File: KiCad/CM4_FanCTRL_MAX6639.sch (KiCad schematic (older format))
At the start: 14 parts, among them M1 Fan_CPU_4pin, M2 Fan_CPU_4pin, U1 MAX6639ATE+

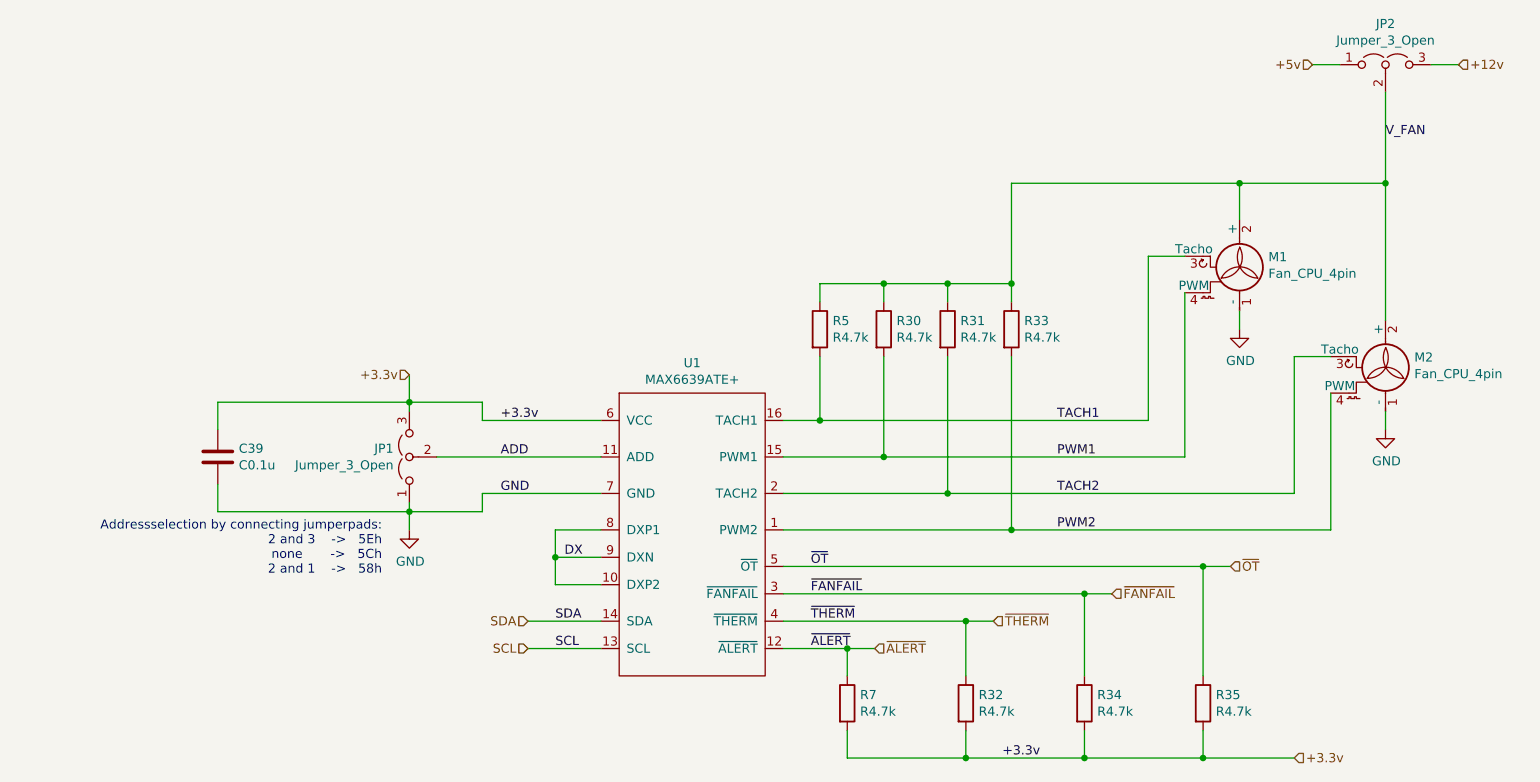
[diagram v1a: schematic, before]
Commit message: PCIe Wiring, resistor value adjustments, and a bunch of small ERC fixes.
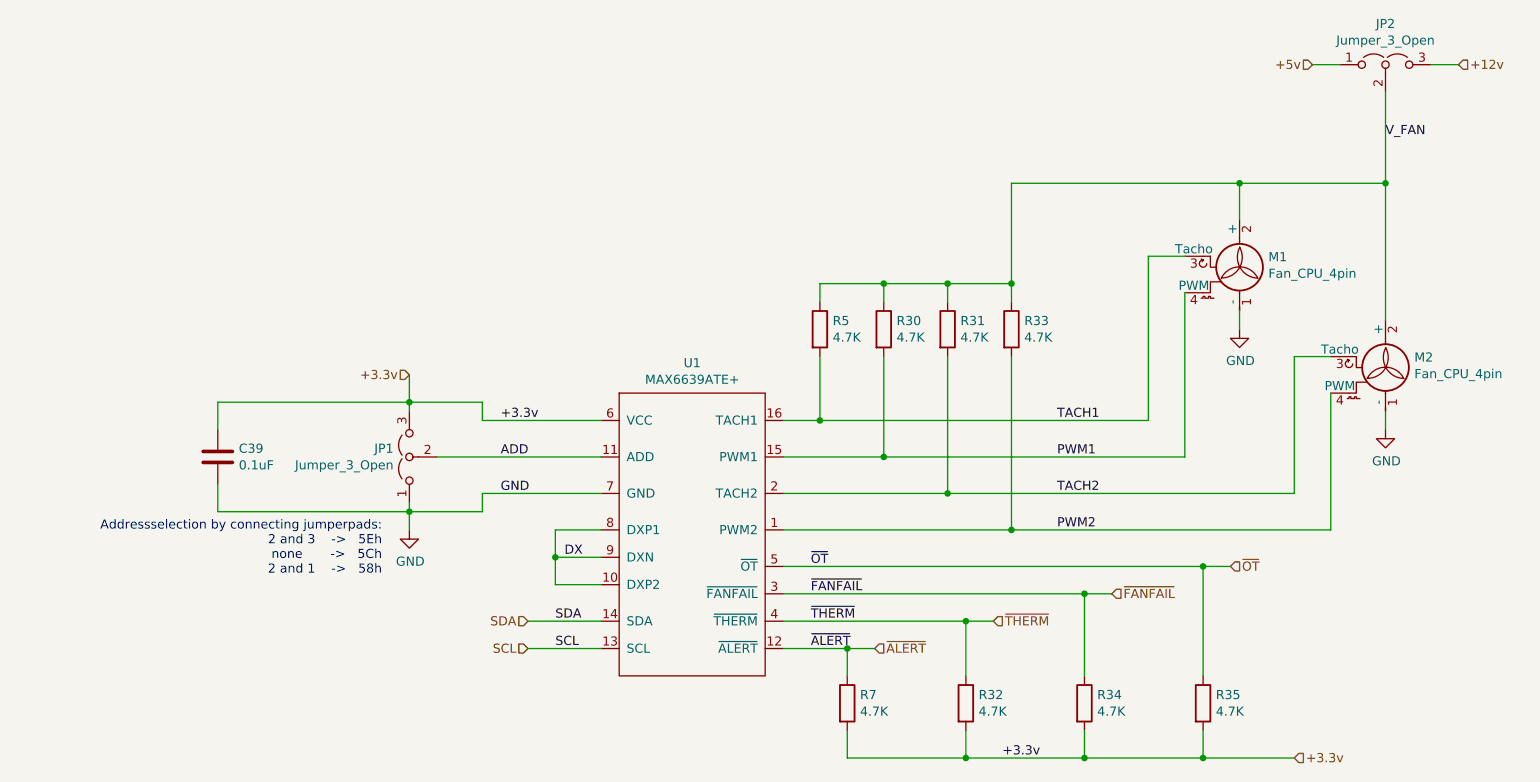
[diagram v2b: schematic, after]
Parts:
- C39: value C0.1u -> 0.1uF
- R30, R31, R32, R33, R34, R35, R5, R7: value R4.7k -> 4.7K
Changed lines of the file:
@@
 P 5750 5350
 F 0 "R7" H 5820 5396 50  0000 L CNN
-F 1 "R4.7k" H 5820 5305 50  0000 L CNN
+F 1 "4.7K" H 5820 5305 50  0000 L CNN
 F 2 "CM4_MATX:R_0805_2012Metric_Pad1.20x1.40mm_HandSolder" V 5680 5350 50  0001 C CNN
 F 3 "~" H 5750 5350 50  0001 C CNN
@@
 P 6400 5350
 F 0 "R32" H 6470 5396 50  0000 L CNN
-F 1 "R4.7k" H 6470 5305 50  0000 L CNN
+F 1 "4.7K" H 6470 5305 50  0000 L CNN
 F 2 "CM4_MATX:R_0805_2012Metric_Pad1.20x1.40mm_HandSolder" V 6330 5350 50  0001 C CNN
 F 3 "~" H 6400 5350 50  0001 C CNN
@@
 P 7050 5350
 F 0 "R34" H 7120 5396 50  0000 L CNN
-F 1 "R4.7k" H 7120 5305 50  0000 L CNN
+F 1 "4.7K" H 7120 5305 50  0000 L CNN
 F 2 "CM4_MATX:R_0805_2012Metric_Pad1.20x1.40mm_HandSolder" V 6980 5350 50  0001 C CNN
 F 3 "~" H 7050 5350 50  0001 C CNN
@@
 P 7700 5350
 F 0 "R35" H 7770 5396 50  0000 L CNN
-F 1 "R4.7k" H 7770 5305 50  0000 L CNN
+F 1 "4.7K" H 7770 5305 50  0000 L CNN
 F 2 "CM4_MATX:R_0805_2012Metric_Pad1.20x1.40mm_HandSolder" V 7630 5350 50  0001 C CNN
 F 3 "~" H 7700 5350 50  0001 C CNN
@@
 P 6300 3300
 F 0 "R31" H 6370 3346 50  0000 L CNN
-F 1 "R4.7k" H 6370 3255 50  0000 L CNN
+F 1 "4.7K" H 6370 3255 50  0000 L CNN
 F 2 "CM4_MATX:R_0805_2012Metric_Pad1.20x1.40mm_HandSolder" V 6230 3300 50  0001 C CNN
 F 3 "~" H 6300 3300 50  0001 C CNN
@@
 P 6650 3300
 F 0 "R33" H 6720 3346 50  0000 L CNN
-F 1 "R4.7k" H 6720 3255 50  0000 L CNN
+F 1 "4.7K" H 6720 3255 50  0000 L CNN
 F 2 "CM4_MATX:R_0805_2012Metric_Pad1.20x1.40mm_HandSolder" V 6580 3300 50  0001 C CNN
 F 3 "~" H 6650 3300 50  0001 C CNN
@@
 P 5600 3300
 F 0 "R5" H 5670 3346 50  0000 L CNN
-F 1 "R4.7k" H 5670 3255 50  0000 L CNN
+F 1 "4.7K" H 5670 3255 50  0000 L CNN
 F 2 "CM4_MATX:R_0805_2012Metric_Pad1.20x1.40mm_HandSolder" V 5530 3300 50  0001 C CNN
 F 3 "~" H 5600 3300 50  0001 C CNN
@@
 P 5950 3300
 F 0 "R30" H 6020 3346 50  0000 L CNN
-F 1 "R4.7k" H 6020 3255 50  0000 L CNN
+F 1 "4.7K" H 6020 3255 50  0000 L CNN
 F 2 "CM4_MATX:R_0805_2012Metric_Pad1.20x1.40mm_HandSolder" V 5880 3300 50  0001 C CNN
 F 3 "~" H 5950 3300 50  0001 C CNN
@@
 P 2300 4000
 F 0 "C39" H 2415 4046 50  0000 L CNN
-F 1 "C0.1u" H 2415 3955 50  0000 L CNN
+F 1 "0.1uF" H 2415 3955 50  0000 L CNN
 F 2 "CM4_MATX:C_0805_2012Metric_Pad1.18x1.45mm_HandSolder" H 2338 3850 50  0001 C CNN
 F 3 "~" H 2300 4000 50  0001 C CNN

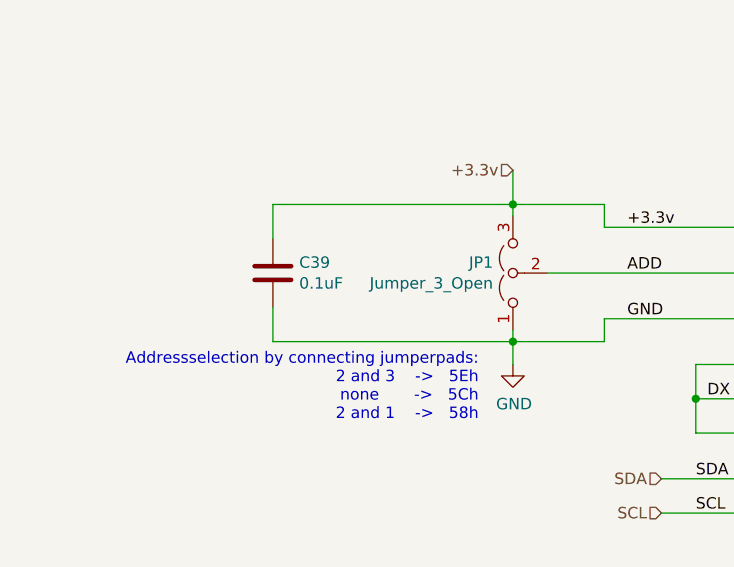
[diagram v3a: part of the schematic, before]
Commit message: Started picking passive components, overhauled library
Cleaned up a bunch of schematic library references.
Added datasheets, descriptions for a lot of existing parts.
Picked most capacitor parts, still a couple left.
Cleaned up a fair few footprint references.
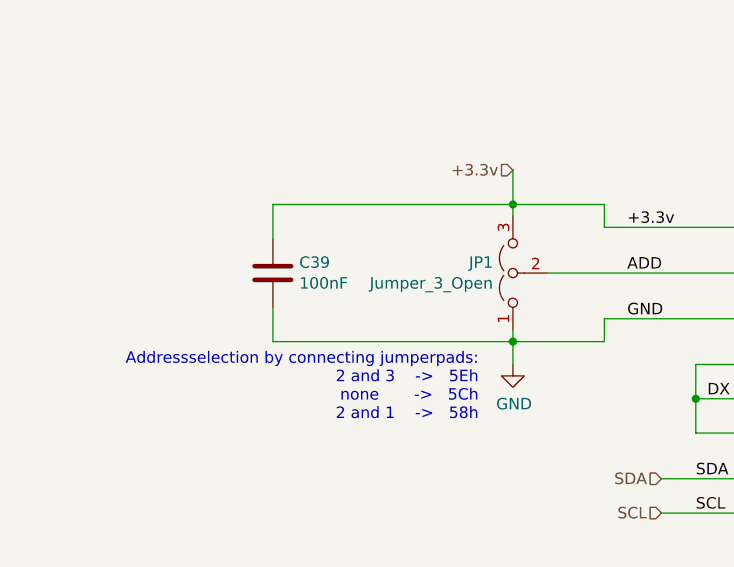
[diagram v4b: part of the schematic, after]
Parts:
- C39: value 0.1uF -> 100nF; footprint CM4_MATX:C_0805_2012Metric_Pad1.18x1.45mm_HandSolder -> CM4_MATX:C_0402_1005Metric_Pad0.74x0.62mm_HandSolder; Description (none) -> 10V 0.1uF X5R 0402 20% Tol; Mfr. (none) -> AVX; Mfr. No (none) -> 0402ZD104MAT4A; Mouser Part Number (none) -> 581-0402ZD104MAT4A; Mouser Price/Stock (none) -> https://www.mouser.co.uk/ProductDetail/AVX/0402ZD104MAT4A/?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
- JP1, JP2: Description (none) -> Standard 2.54mm (100mil)-separated pins
- U1: Description (none) -> 2-Channel Temperature Monitor with Dual, Automatic, PWM Fan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; Mfr. No (none) -> MAX6639ATE+; Mfr. No. MAX6639ATE+ -> (none); Mouser No. 700-MAX6639ATE -> (none); Mouser Part Number (none) -> 700-MAX6639ATE; Mouser Price/Stock (none) -> https://www.mouser.co.uk/ProductDetail/Maxim-Integrated/MAX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
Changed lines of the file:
@@
 F 2 "CM4_MATX:TQFN-16-1EP_5x5mm_P0.8mm_EP3.1x3.1mm" H 4950 5800 50  0001 C CNN
 F 3 "https://datasheets.maximintegrated.com/en/ds/MAX6639-MAX6639F.pdf" H 4900 5500 50  0001 C CNN
-F 4 "700-MAX6639ATE" H 4900 5700 50  0001 C CNN "Mouser No."
-F 5 "Maxim Integrated" H 4900 5700 50  0001 C CNN "Mfr."
-F 6 "MAX6639ATE+" H 4900 5350 50  0001 C CNN "Mfr. No."
+F 4 "Maxim Integrated" H 4900 5700 50  0001 C CNN "Mfr."
+F 5 "MAX6639ATE+" H 4900 4450 50  0001 C CNN "Mfr. No"
+F 6 "700-MAX6639ATE" H 4900 4450 50  0001 C CNN "Mouser Part Number"
+F 7 "https://www.mouser.co.uk/ProductDetail/Maxim-Integrated/MAX6639ATE%2b/?qs=7H2Jq%252ByxpJLsoVNJxdDPow%3D%3D" H 4900 4450 50  0001 C CNN "Mouser Price/Stock"
+F 8 "2-Channel Temperature Monitor with Dual, Automatic, PWM Fan-Speed Controller" H 4900 4450 50  0001 C CNN "Description"
 	1    4900 4450
 	1    0    0    -1
@@
 P 2300 4000
 F 0 "C39" H 2415 4046 50  0000 L CNN
-F 1 "0.1uF" H 2415 3955 50  0000 L CNN
-F 2 "CM4_MATX:C_0805_2012Metric_Pad1.18x1.45mm_HandSolder" H 2338 3850 50  0001 C CNN
-F 3 "~" H 2300 4000 50  0001 C CNN
+F 1 "100nF" H 2415 3955 50  0000 L CNN
+F 2 "CM4_MATX:C_0402_1005Metric_Pad0.74x0.62mm_HandSolder" H 2338 3850 50  0001 C CNN
+F 3 "https://www.mouser.co.uk/datasheet/2/40/cx5r-776519.pdf" H 2300 4000 50  0001 C CNN
+F 4 "581-0402ZD104MAT4A" H 2300 4000 50  0001 C CNN "Mouser Part Number"
+F 5 "https://www.mouser.co.uk/ProductDetail/AVX/0402ZD104MAT4A/?qs=sGAEpiMZZMvsSlwiRhF8qud6rLLpfNdE%2FYSoyEGdkn4%3D" H 2300 4000 50  0001 C CNN "Mouser Price/Stock"
+F 6 "AVX" H 2300 4000 50  0001 C CNN "Mfr."
+F 7 "0402ZD104MAT4A" H 2300 4000 50  0001 C CNN "Mfr. No"
+F 8 "10V 0.1uF X5R 0402 20% Tol" H 2300 4000 50  0001 C CNN "Description"
 	1    2300 4000
 	1    0    0    -1
@@
 F 2 "CM4_MATX:PinHeader_1x03_P2.54mm_Vertical" H 3350 4000 50  0001 C CNN
 F 3 "~" H 3350 4000 50  0001 C CNN
+F 4 "Standard 2.54mm (100mil)-separated pins" H 3350 4000 50  0001 C CNN "Description"
 	1    3350 4000
 	0    -1   -1   0
@@
 F 2 "CM4_MATX:PinHeader_1x03_P2.54mm_Vertical" H 8700 1850 50  0001 C CNN
 F 3 "~" H 8700 1850 50  0001 C CNN
+F 4 "Standard 2.54mm (100mil)-separated pins" H 8700 1850 50  0001 C CNN "Description"
 	1    8700 1850
 	1    0    0    -1

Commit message: More BOM changes
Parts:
- M1, M2: Description (none) -> Standard PC 4-pin fan header (Molex 47053-100); Mfr. (none) -> Molex; Mfr. No (none) -> 47053-1000; Mouser Part Number (none) -> 538-47053-1000; Mouser Price/Stock (none) -> https://www.mouser.co.uk/ProductDetail/Molex/47053-1000/?qs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
- R30, R31, R32, R33, R34, R35, R5, R7: footprint CM4_MATX:R_0805_2012Metric_Pad1.20x1.40mm_HandSolder -> CM4_MATX:R_0402_1005Metric_Pad0.72x0.64mm_HandSolder; Description (none) -> 0402 1/16W 4.7KOhm 1%; Mfr. (none) -> Yageo; Mfr. No (none) -> RC0402FR-074K7L; Mouser Part Number (none) -> 603-RC0402FR-074K7L; Mouser Price/Stock (none) -> https://www.mouser.co.uk/ProductDetail/Yageo/RC0402FR-074K7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
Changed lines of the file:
@@
 F 0 "R7" H 5820 5396 50  0000 L CNN
 F 1 "4.7K" H 5820 5305 50  0000 L CNN
-F 2 "CM4_MATX:R_0805_2012Metric_Pad1.20x1.40mm_HandSolder" V 5680 5350 50  0001 C CNN
-F 3 "~" H 5750 5350 50  0001 C CNN
+F 2 "CM4_MATX:R_0402_1005Metric_Pad0.72x0.64mm_HandSolder" V 5680 5350 50  0001 C CNN
+F 3 "https://www.mouser.co.uk/datasheet/2/447/PYu_RC_Group_51_RoHS_L_10-1664068.pdf" H 5750 5350 50  0001 C CNN
+F 4 "0402 1/16W 4.7KOhm 1%" H 5750 5350 50  0001 C CNN "Description"
+F 5 "Yageo" H 5750 5350 50  0001 C CNN "Mfr."
+F 6 "RC0402FR-074K7L" H 5750 5350 50  0001 C CNN "Mfr. No"
+F 7 "603-RC0402FR-074K7L" H 5750 5350 50  0001 C CNN "Mouser Part Number"
+F 8 "https://www.mouser.co.uk/ProductDetail/Yageo/RC0402FR-074K7L/?qs=sGAEpiMZZMvdGkrng054t8Tx25L%252BvTaRRFeij8HQtRc%3D" H 5750 5350 50  0001 C CNN "Mouser Price/Stock"
 	1    5750 5350
 	1    0    0    -1
@@
 F 0 "R32" H 6470 5396 50  0000 L CNN
 F 1 "4.7K" H 6470 5305 50  0000 L CNN
-F 2 "CM4_MATX:R_0805_2012Metric_Pad1.20x1.40mm_HandSolder" V 6330 5350 50  0001 C CNN
-F 3 "~" H 6400 5350 50  0001 C CNN
+F 2 "CM4_MATX:R_0402_1005Metric_Pad0.72x0.64mm_HandSolder" V 6330 5350 50  0001 C CNN
+F 3 "https://www.mouser.co.uk/datasheet/2/447/PYu_RC_Group_51_RoHS_L_10-1664068.pdf" H 6400 5350 50  0001 C CNN
+F 4 "0402 1/16W 4.7KOhm 1%" H 6400 5350 50  0001 C CNN "Description"
+F 5 "Yageo" H 6400 5350 50  0001 C CNN "Mfr."
+F 6 "RC0402FR-074K7L" H 6400 5350 50  0001 C CNN "Mfr. No"
+F 7 "603-RC0402FR-074K7L" H 6400 5350 50  0001 C CNN "Mouser Part Number"
+F 8 "https://www.mouser.co.uk/ProductDetail/Yageo/RC0402FR-074K7L/?qs=sGAEpiMZZMvdGkrng054t8Tx25L%252BvTaRRFeij8HQtRc%3D" H 6400 5350 50  0001 C CNN "Mouser Price/Stock"
 	1    6400 5350
 	1    0    0    -1
@@
 F 0 "R34" H 7120 5396 50  0000 L CNN
 F 1 "4.7K" H 7120 5305 50  0000 L CNN
-F 2 "CM4_MATX:R_0805_2012Metric_Pad1.20x1.40mm_HandSolder" V 6980 5350 50  0001 C CNN
-F 3 "~" H 7050 5350 50  0001 C CNN
+F 2 "CM4_MATX:R_0402_1005Metric_Pad0.72x0.64mm_HandSolder" V 6980 5350 50  0001 C CNN
+F 3 "https://www.mouser.co.uk/datasheet/2/447/PYu_RC_Group_51_RoHS_L_10-1664068.pdf" H 7050 5350 50  0001 C CNN
+F 4 "0402 1/16W 4.7KOhm 1%" H 7050 5350 50  0001 C CNN "Description"
+F 5 "Yageo" H 7050 5350 50  0001 C CNN "Mfr."
+F 6 "RC0402FR-074K7L" H 7050 5350 50  0001 C CNN "Mfr. No"
+F 7 "603-RC0402FR-074K7L" H 7050 5350 50  0001 C CNN "Mouser Part Number"
+F 8 "https://www.mouser.co.uk/ProductDetail/Yageo/RC0402FR-074K7L/?qs=sGAEpiMZZMvdGkrng054t8Tx25L%252BvTaRRFeij8HQtRc%3D" H 7050 5350 50  0001 C CNN "Mouser Price/Stock"
 	1    7050 5350
 	1    0    0    -1
@@
 F 0 "R35" H 7770 5396 50  0000 L CNN
 F 1 "4.7K" H 7770 5305 50  0000 L CNN
-F 2 "CM4_MATX:R_0805_2012Metric_Pad1.20x1.40mm_HandSolder" V 7630 5350 50  0001 C CNN
-F 3 "~" H 7700 5350 50  0001 C CNN
+F 2 "CM4_MATX:R_0402_1005Metric_Pad0.72x0.64mm_HandSolder" V 7630 5350 50  0001 C CNN
+F 3 "https://www.mouser.co.uk/datasheet/2/447/PYu_RC_Group_51_RoHS_L_10-1664068.pdf" H 7700 5350 50  0001 C CNN
+F 4 "0402 1/16W 4.7KOhm 1%" H 7700 5350 50  0001 C CNN "Description"
+F 5 "Yageo" H 7700 5350 50  0001 C CNN "Mfr."
+F 6 "RC0402FR-074K7L" H 7700 5350 50  0001 C CNN "Mfr. No"
+F 7 "603-RC0402FR-074K7L" H 7700 5350 50  0001 C CNN "Mouser Part Number"
+F 8 "https://www.mouser.co.uk/ProductDetail/Yageo/RC0402FR-074K7L/?qs=sGAEpiMZZMvdGkrng054t8Tx25L%252BvTaRRFeij8HQtRc%3D" H 7700 5350 50  0001 C CNN "Mouser Price/Stock"
 	1    7700 5350
 	1    0    0    -1
@@
 F 0 "R31" H 6370 3346 50  0000 L CNN
 F 1 "4.7K" H 6370 3255 50  0000 L CNN
-F 2 "CM4_MATX:R_0805_2012Metric_Pad1.20x1.40mm_HandSolder" V 6230 3300 50  0001 C CNN
-F 3 "~" H 6300 3300 50  0001 C CNN
+F 2 "CM4_MATX:R_0402_1005Metric_Pad0.72x0.64mm_HandSolder" V 6230 3300 50  0001 C CNN
+F 3 "https://www.mouser.co.uk/datasheet/2/447/PYu_RC_Group_51_RoHS_L_10-1664068.pdf" H 6300 3300 50  0001 C CNN
+F 4 "0402 1/16W 4.7KOhm 1%" H 6300 3300 50  0001 C CNN "Description"
+F 5 "Yageo" H 6300 3300 50  0001 C CNN "Mfr."
+F 6 "RC0402FR-074K7L" H 6300 3300 50  0001 C CNN "Mfr. No"
+F 7 "603-RC0402FR-074K7L" H 6300 3300 50  0001 C CNN "Mouser Part Number"
+F 8 "https://www.mouser.co.uk/ProductDetail/Yageo/RC0402FR-074K7L/?qs=sGAEpiMZZMvdGkrng054t8Tx25L%252BvTaRRFeij8HQtRc%3D" H 6300 3300 50  0001 C CNN "Mouser Price/Stock"
 	1    6300 3300
 	1    0    0    -1
@@
 F 0 "R33" H 6720 3346 50  0000 L CNN
 F 1 "4.7K" H 6720 3255 50  0000 L CNN
-F 2 "CM4_MATX:R_0805_2012Metric_Pad1.20x1.40mm_HandSolder" V 6580 3300 50  0001 C CNN
-F 3 "~" H 6650 3300 50  0001 C CNN
+F 2 "CM4_MATX:R_0402_1005Metric_Pad0.72x0.64mm_HandSolder" V 6580 3300 50  0001 C CNN
+F 3 "https://www.mouser.co.uk/datasheet/2/447/PYu_RC_Group_51_RoHS_L_10-1664068.pdf" H 6650 3300 50  0001 C CNN
+F 4 "0402 1/16W 4.7KOhm 1%" H 6650 3300 50  0001 C CNN "Description"
+F 5 "Yageo" H 6650 3300 50  0001 C CNN "Mfr."
+F 6 "RC0402FR-074K7L" H 6650 3300 50  0001 C CNN "Mfr. No"
+F 7 "603-RC0402FR-074K7L" H 6650 3300 50  0001 C CNN "Mouser Part Number"
+F 8 "https://www.mouser.co.uk/ProductDetail/Yageo/RC0402FR-074K7L/?qs=sGAEpiMZZMvdGkrng054t8Tx25L%252BvTaRRFeij8HQtRc%3D" H 6650 3300 50  0001 C CNN "Mouser Price/Stock"
 	1    6650 3300
 	1    0    0    -1
@@
 F 0 "R5" H 5670 3346 50  0000 L CNN
 F 1 "4.7K" H 5670 3255 50  0000 L CNN
-F 2 "CM4_MATX:R_0805_2012Metric_Pad1.20x1.40mm_HandSolder" V 5530 3300 50  0001 C CNN
-F 3 "~" H 5600 3300 50  0001 C CNN
+F 2 "CM4_MATX:R_0402_1005Metric_Pad0.72x0.64mm_HandSolder" V 5530 3300 50  0001 C CNN
+F 3 "https://www.mouser.co.uk/datasheet/2/447/PYu_RC_Group_51_RoHS_L_10-1664068.pdf" H 5600 3300 50  0001 C CNN
+F 4 "0402 1/16W 4.7KOhm 1%" H 5600 3300 50  0001 C CNN "Description"
+F 5 "Yageo" H 5600 3300 50  0001 C CNN "Mfr."
+F 6 "RC0402FR-074K7L" H 5600 3300 50  0001 C CNN "Mfr. No"
+F 7 "603-RC0402FR-074K7L" H 5600 3300 50  0001 C CNN "Mouser Part Number"
+F 8 "https://www.mouser.co.uk/ProductDetail/Yageo/RC0402FR-074K7L/?qs=sGAEpiMZZMvdGkrng054t8Tx25L%252BvTaRRFeij8HQtRc%3D" H 5600 3300 50  0001 C CNN "Mouser Price/Stock"
 	1    5600 3300
 	1    0    0    -1
@@
 F 0 "R30" H 6020 3346 50  0000 L CNN
 F 1 "4.7K" H 6020 3255 50  0000 L CNN
-F 2 "CM4_MATX:R_0805_2012Metric_Pad1.20x1.40mm_HandSolder" V 5880 3300 50  0001 C CNN
-F 3 "~" H 5950 3300 50  0001 C CNN
+F 2 "CM4_MATX:R_0402_1005Metric_Pad0.72x0.64mm_HandSolder" V 5880 3300 50  0001 C CNN
+F 3 "https://www.mouser.co.uk/datasheet/2/447/PYu_RC_Group_51_RoHS_L_10-1664068.pdf" H 5950 3300 50  0001 C CNN
+F 4 "0402 1/16W 4.7KOhm 1%" H 5950 3300 50  0001 C CNN "Description"
+F 5 "Yageo" H 5950 3300 50  0001 C CNN "Mfr."
+F 6 "RC0402FR-074K7L" H 5950 3300 50  0001 C CNN "Mfr. No"
+F 7 "603-RC0402FR-074K7L" H 5950 3300 50  0001 C CNN "Mouser Part Number"
+F 8 "https://www.mouser.co.uk/ProductDetail/Yageo/RC0402FR-074K7L/?qs=sGAEpiMZZMvdGkrng054t8Tx25L%252BvTaRRFeij8HQtRc%3D" H 5950 3300 50  0001 C CNN "Mouser Price/Stock"
 	1    5950 3300
 	1    0    0    -1
@@
 F 2 "CM4_MATX:FanPinHeader_1x04_P2.54mm_Vertical" H 7950 2460 50  0001 C CNN
 F 3 "http://www.formfactors.org/developer%5Cspecs%5Crev1_2_public.pdf" H 7900 3010 50  0001 C CNN
+F 4 "Standard PC 4-pin fan header (Molex 47053-100)" H 7900 3000 50  0001 C CNN "Description"
+F 5 "Molex" H 7900 3000 50  0001 C CNN "Mfr."
+F 6 "47053-1000" H 7900 3000 50  0001 C CNN "Mfr. No"
+F 7 "538-47053-1000" H 7900 3000 50  0001 C CNN "Mouser Part Number"
+F 8 "https://www.mouser.co.uk/ProductDetail/Molex/47053-1000/?qs=ph4zPCVRuvqoDX7hrEhxNA%3D%3D" H 7900 3000 50  0001 C CNN "Mouser Price/Stock"
 	1    7900 3000
 	1    0    0    -1
@@
 F 2 "CM4_MATX:FanPinHeader_1x04_P2.54mm_Vertical" H 8750 3010 50  0001 C CNN
 F 3 "http://www.formfactors.org/developer%5Cspecs%5Crev1_2_public.pdf" H 8700 3560 50  0001 C CNN
+F 4 "Standard PC 4-pin fan header (Molex 47053-100)" H 8700 3550 50  0001 C CNN "Description"
+F 5 "Molex" H 8700 3550 50  0001 C CNN "Mfr."
+F 6 "47053-1000" H 8700 3550 50  0001 C CNN "Mfr. No"
+F 7 "538-47053-1000" H 8700 3550 50  0001 C CNN "Mouser Part Number"
+F 8 "https://www.mouser.co.uk/ProductDetail/Molex/47053-1000/?qs=ph4zPCVRuvqoDX7hrEhxNA%3D%3D" H 8700 3550 50  0001 C CNN "Mouser Price/Stock"
 	1    8700 3550
 	1    0    0    -1

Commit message: Connected all grounds in the schematic and planes
Planes:
In 1 - Ground
In 2 - 3.3v Zone which excludes the IO and 5v Zone around only the IO
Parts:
- added GND (x2): GND, symbol CM4_MATX:GND
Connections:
- net GND: now also GND.1 (GND), GND.1 (GND)
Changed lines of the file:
@@
 $EndComp
 $Comp
-L CM4_MATX:GND #PWR0202
+L CM4_MATX:GND GND
 U 1 1 5FF2AB5B
 P 7900 3300
-F 0 "#PWR0202" H 7900 3050 50  0001 C CNN
+F 0 "GND" H 7900 3050 50  0001 C CNN
 F 1 "GND" H 7905 3127 50  0000 C CNN
 F 2 "" H 7900 3300 50  0001 C CNN
@@
 $EndComp
 $Comp
-L CM4_MATX:GND #PWR0203
+L CM4_MATX:GND GND
 U 1 1 5FF2C109
 P 8700 3850
-F 0 "#PWR0203" H 8700 3600 50  0001 C CNN
+F 0 "GND" H 8700 3600 50  0001 C CNN
 F 1 "GND" H 8705 3677 50  0000 C CNN
 F 2 "" H 8700 3850 50  0001 C CNN
